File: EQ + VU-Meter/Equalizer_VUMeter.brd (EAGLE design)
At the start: 116 x 38.7 mm, 220 parts, among them IC1 TL074D, IC2 TL074D, IC3 TL074D, IC4 TL074D, T1 BC846A, T10 BC846A, T11 BC846A, T12 BC846A, T13 BC846A, T14 BC846A, T15 BC846A, T16 BC846A, T17 BC846A, T18 BC846A, T19 BC846A, T2 BC846A, T20 BC846A, T21 BC846A, T22 BC846A, T23 BC846A, T24 BC846A, T25 BC846A, T26 BC846A, T27 BC846A, T28 BC846A, T29 BC846A, T3 BC846A, T30 BC846A, T4 BC846A, T5 BC846A, T6 BC846A, T7 BC846A, T8 BC846A, T9 BC846A

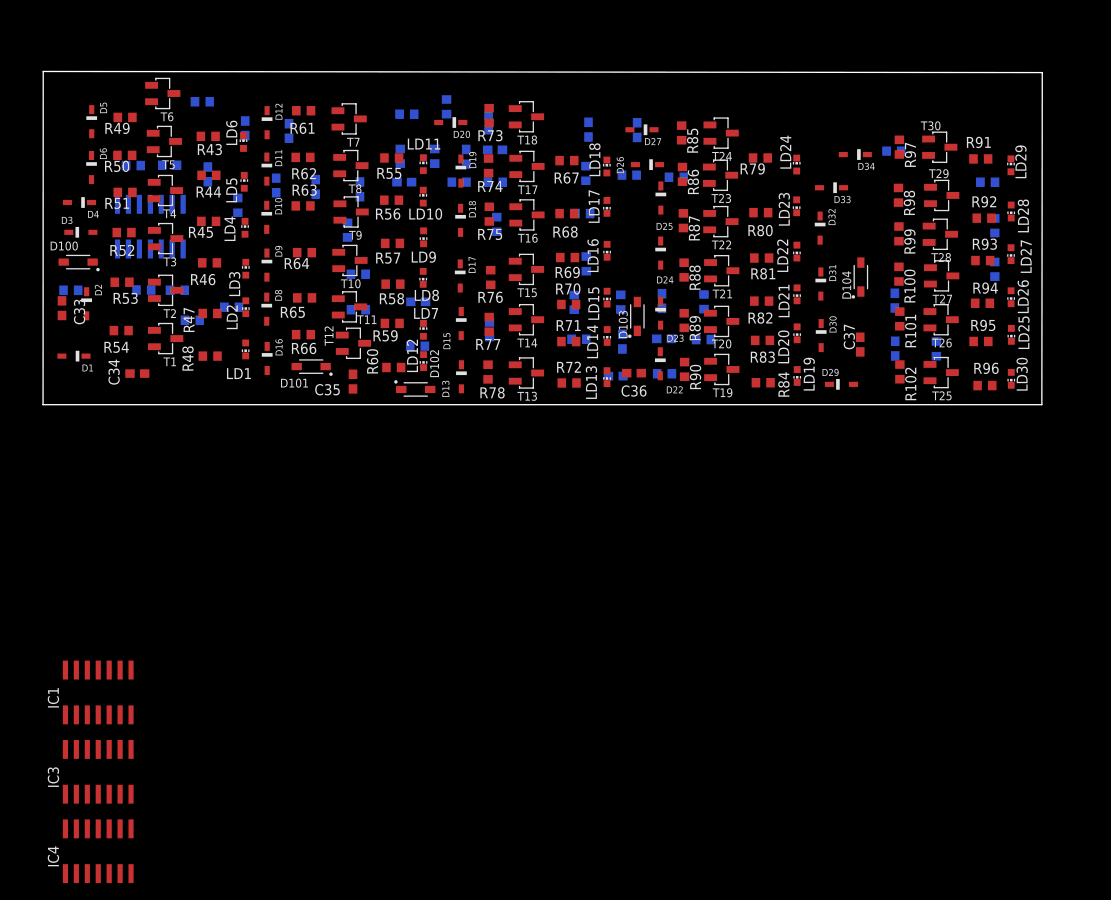
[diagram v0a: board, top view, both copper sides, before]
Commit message: # Mainboard updated
# Keyboard V2:

	# Bug fixed (lowest Pad not GND)
	# 1 more key (upper C)
	# PEACE sign corrected

# General cleanup
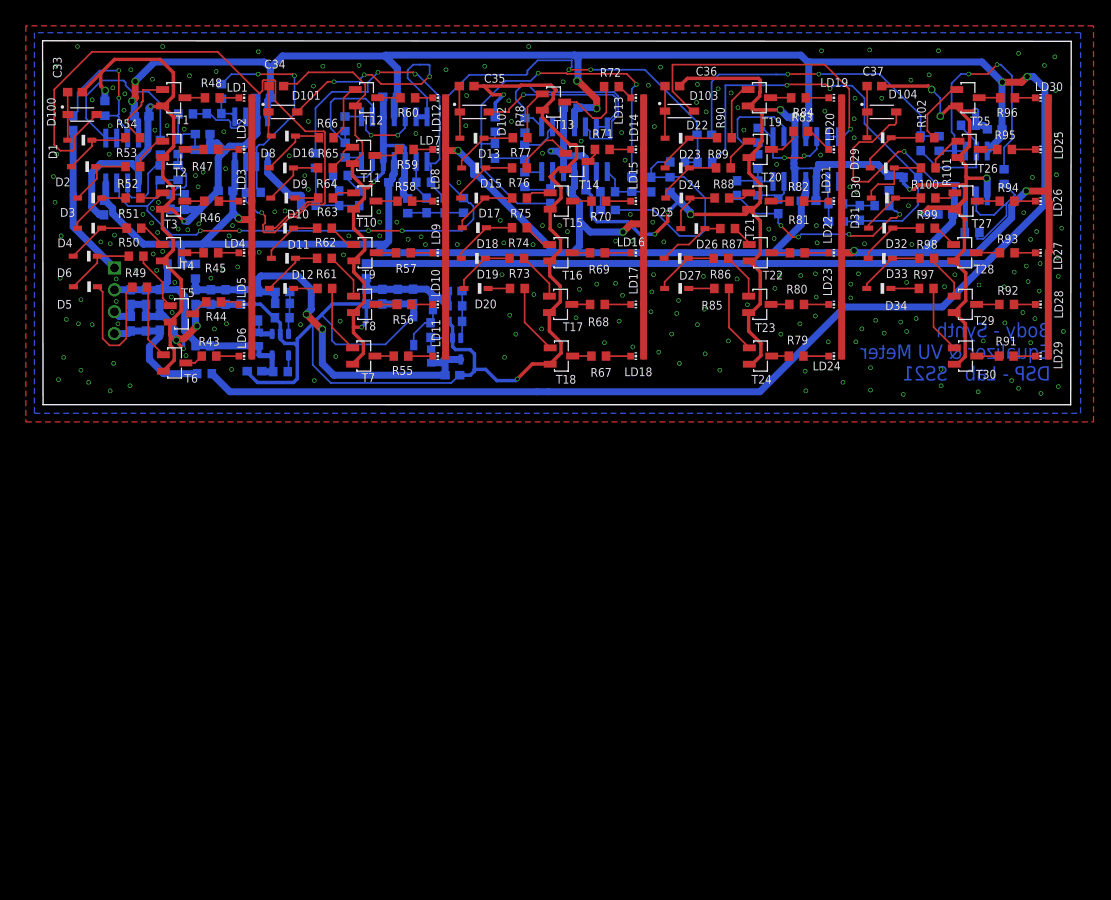
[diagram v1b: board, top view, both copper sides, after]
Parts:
- added C10, C11, C12, C13, C27, C28, C29, C32, C39, C4, C8, C9: 100n, rcl:C0603
- added C14, C40, C41, C42, C43, C44, C45, C46, C47, C48, C49, C50: 10u, rcl:C0603
- added C5: 2.2 uF, rcl:C0603
- added C7: 4.7 uF, rcl:C0603
- added CCUK: 1 uF, rcl:C0603
- added CF: 220 pF, rcl:C0603
- added CFF: 330 pF, rcl:C0603
- added CIN, COUT: 22 uF, rcl:C0603
- added D14, D7: (no value), MMSZ5226B-7-F:SOD3715X135L32X57N
- added IC5, IC7: TL072D, linear:SO08
- added J2: 640455-4, 640455-4:TE_640455-4
- added L1, L2, L3: 10 uH, ASMCI-0603-100M-T:INDC1608X95N
- added R103, R104, R105: 0, rcl:R0603
- added R31: 68 K, rcl:R0603
- added R32: 51K, rcl:R0603
- added R35: 13.3K, rcl:R0603
- added R41: 3.3k, rcl:R0603
- added R42: 35K, rcl:R0603
- added RFB1: 29.4K, rcl:R0603
- added RFB2: 5.76K, rcl:R0603
- added U1: LM2611, LM2611BMFX_NOPB:SOT95P280X145-5N
- added U2: LMR62014, LMR62014XMF_NOPB:SOT95P280X145-5N
- IC1: value TL074D -> TL072D; device linear:SO14 -> linear:SO08
- R26: value 3.3k -> 0
- R27: value 35K -> 0
- moved IC4 115.0 mm to (88.6, 28.5), flipped to the bottom
- moved IC3 91.0 mm to (61.7, 29.7), flipped to the bottom
- moved R27 82.3 mm to (17.7, 15.5), turned to 90 degrees
- moved IC1 66.7 mm to (24.2, 30.8), flipped to the bottom, turned to 180 degrees
- moved R26 45.5 mm to (18.6, 6.85), turned to 180 degrees
- moved R34 41.7 mm to (100.8, 26.4), turned to 180 degrees
- moved C34 37.1 mm to (27.1, 37.0)
- moved C35 36.8 mm to (49.2, 37.0), turned to 0 degrees
- moved R72 34.8 mm to (66.0, 36.9)
- moved R37 34.2 mm to (98.3, 25.7), turned to 270 degrees
- moved C36 33.6 mm to (73.1, 37.0), turned to 0 degrees
- moved R96 33.5 mm to (112.0, 35.6)
- moved R84 33.3 mm to (87.7, 35.6)
- moved D102 32.9 mm to (50.1, 34.0)
- moved LD30 32.8 mm to (116.0, 35.6), turned to 90 degrees
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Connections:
- removed net +8V: IC1.4, IC2.4, IC3.4, IC4.4, LD1.A, LD10.A, LD11.A, LD12.A, LD13.A, LD14.A, LD15.A, LD16.A, LD17.A, LD18.A, LD19.A, LD2.A, LD20.A, LD21.A, LD22.A, LD23.A, LD24.A, LD25.A, LD26.A, LD27.A, LD28.A, LD29.A, LD3.A, LD30.A, LD4.A, LD5.A, LD6.A, LD7.A, LD8.A, LD9.A
- removed net -8V: IC1.11, IC2.11, IC3.11, IC4.11
- removed net 3.3V: C38.2
- removed net N$1: C2.1, C3.1
- removed net N$14: IC3.13, R26.2, R27.1
- removed net N$6: C1.1, C6.1
- removed net TP_OUT1: IC2.8, R6.2
- removed net TP_OUT2: IC3.7, R25.2
- removed net TP_OUT3: IC3.14, R27.2
- new net +7,5V: C45.2, C46.1, C47.1, C7.1, CF.1, CIN.1, D7.1, L2.1, R27.1, R31.2, U1.4, U1.5
- new net -7,5V: C48.2, C49.1, C50.1, CFF.1, COUT.1, L3.2, R105.1, RFB1.1
- new net IN2,1V: C38.2, J2.1
- new net MAIN-5V: C14.2, C43.1, C44.1, J2.4, R103.1
- new net N$100: IC3.12, IC3.8, R25.2
- new net N$115: IC2.12, IC2.8, R6.2
- new net N$126: CCUK.2, D14.2, L3.1
- new net N$141: CCUK.1, L2.2, U1.1
- new net N$152: CFF.2, RFB1.2, RFB2.1, U1.3
- new net N$16: C17.1, R29.2
- new net N$18: C21.1, IC3.7, R18.2, R19.1
- new net N$181: IC2.7, R3.1
- new net N$183: IC4.9, R41.2, R42.1
- new net N$21: R32.1, U2.4
- new net N$22: CF.2, R31.1, R35.1, U2.3
- new net N$25: IC4.12, IC4.8, R42.2
- new net N$48: C25.1, IC4.7, R38.2, R41.1
- new net N$74: D7.2, L1.2, U2.1
- new net PB5V: C40.2, C41.1, C42.1, C5.1, J2.2, L1.1, R104.2, R26.1, R26.2, R32.2, U2.5
- new net V+: C27.1, C28.1, C29.1, C32.1, C39.1, C9.1, IC1.8, IC2.4, IC3.4, IC4.4, IC5.8, IC7.8, LD1.A, LD10.A, LD11.A, LD12.A, LD13.A, LD14.A, LD15.A, LD16.A, LD17.A, LD18.A, LD19.A, LD2.A, LD20.A, LD21.A, LD22.A, LD23.A, LD24.A, LD25.A, LD26.A, LD27.A, LD28.A, LD29.A, LD3.A, LD30.A, LD4.A, LD5.A, LD6.A, LD7.A, LD8.A, LD9.A, R104.1, R27.2
- new net V-: C10.2, C11.2, C12.2, C13.2, C4.2, C8.2, IC1.4, IC2.11, IC3.11, IC4.11, IC5.4, IC7.4, R103.2, R105.2
- net BP1_OUT: now also IC2.13, IC2.14; no longer C17.1, IC2.7, R29.2, R3.1
- net BP2_OUT: now also IC3.13, IC3.14; no longer C21.1, IC3.1, R18.2, R19.1
- net BP3_OUT: now also IC4.13, IC4.14; no longer C25.1, IC4.1, R26.1, R38.2
- net GND: now also C10.1, C11.1, C12.1, C13.1, C14.1, C27.2, C28.2, C29.2, C32.2, C39.2, C4.1, C40.1, C41.2, C42.2, C43.2, C44.2, C45.1, C46.2, C47.2, C48.1, C49.2, C5.2, C50.2, C7.2, C8.1, C9.2, CIN.2, COUT.2, D14.1, IC1.3, IC4.10, IC5.5, IC7.5, J2.3, R35.2, RFB2.2, U1.2, U2.2; no longer IC1.10, IC1.12, IC2.12, IC3.12
- net HP_OUT: now also IC7.7; no longer IC4.7
- net N$10: now also IC1.6; no longer IC1.13
- net N$19: now also IC3.2; no longer IC2.13
- net N$2: now also C1.1, C6.1
- net N$20: now also IC3.1; no longer IC2.14
- net N$24: now also IC3.6; no longer IC3.2
- net N$26: now also IC4.1; no longer IC3.8
- net N$28: now also IC4.2; no longer IC3.9
- net N$29: now also IC5.6; no longer IC1.6
- net N$3: now also IC1.2; no longer IC1.9
- net N$32: now also IC4.6; no longer IC4.2
- net N$34: now also IC7.3; no longer IC4.10
- net N$36: now also IC7.1, IC7.2; no longer IC4.8, IC4.9
- net N$39: now also IC7.6; no longer IC4.6
- net N$4: now also C2.1, C3.1
- net N$42: now also IC5.1, IC5.2; no longer IC1.1, IC1.2
- net N$47: now also IC5.3; no longer IC1.3
- net N$5: now also IC5.7; no longer IC1.7
- net N$8: now also IC1.1; no longer IC1.8
- net N$9: now also IC3.9; no longer IC3.6
- net TP_OUT: now also IC1.7; no longer IC1.14
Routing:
- net GND: track 0.00 -> 577.5 mm, vias 0 -> 21
- net V+: track 0.00 -> 355.1 mm, vias 0 -> 5
- net V-: track 0.00 -> 352.1 mm, vias 0 -> 6
- net N$5: track 0.00 -> 108.3 mm, vias 0 -> 6
- net TP_OUT: track 0.00 -> 80.9 mm, vias 0 -> 1
- net N$27: track 0.00 -> 51.3 mm, vias 0 -> 2
- net N$23: track 0.00 -> 51.1 mm, vias 0 -> 2
- net +7,5V: track 0.00 -> 50.3 mm, vias 0 -> 2
- net N$38: track 0.00 -> 37.4 mm, vias 0 -> 2
- net N$13: track 0.00 -> 37.0 mm, vias 0 -> 2
- net HP_OUT: track 0.00 -> 36.8 mm, vias 0 -> 1
- net BP3_OUT: track 0.00 -> 36.1 mm, vias 0 -> 1
- net PB5V: track 0.00 -> 31.4 mm
- net N$36: track 0.00 -> 30.8 mm, vias 0 -> 2
- net BP1_OUT: track 0.00 -> 29.9 mm, vias 0 -> 3
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- added copper zone on layer 1, net GND
- added copper zone on layer 16, net GND
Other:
- board size 116 x 38.7 mm -> 119.5 x 42.3 mm
- board text added: "Body - Synth Equalizer & VU Meter DSP - Lab SS21"

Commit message: # Mainboard updated V
# Keys finalizing production
# EQ finalizing production
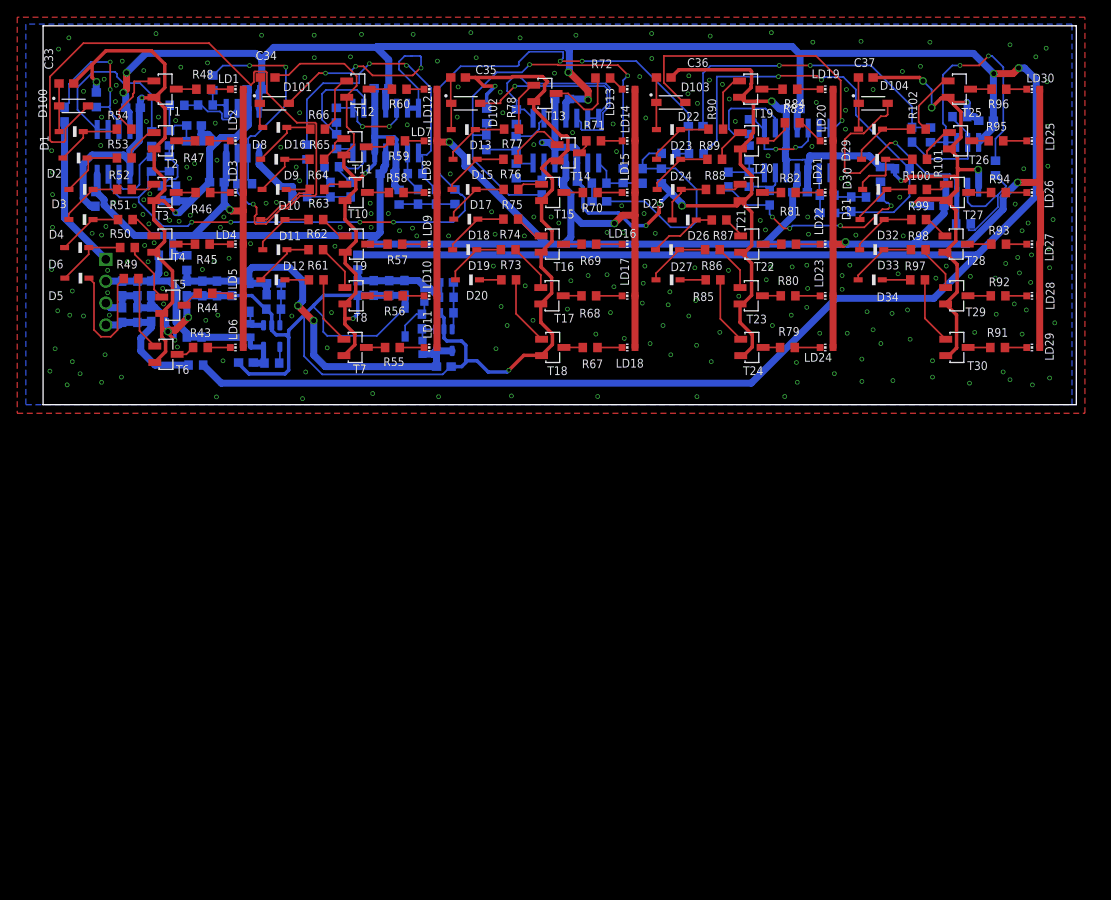
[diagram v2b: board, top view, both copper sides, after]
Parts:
- moved R71 1.41 mm to (63.9, 30.6)
- moved C1 1.41 mm to (17.5, 32.4)
- moved D16 1.41 mm to (26.9, 32.2)
- moved R83 1.41 mm to (87.0, 32.7)
- moved CIN 1.41 mm to (46.5, 4.42)
- moved D1 1.41 mm to (3.27, 31.7)
- moved D2 1.41 mm to (3.71, 28.6)
- moved R32 1.41 mm to (26.6, 4.83)
- moved C10 1.41 mm to (24.6, 36.6)
- moved C11 1.41 mm to (39.3, 36.8)
- moved C12 1.41 mm to (60.3, 35.5)
- moved C13 1.41 mm to (87.1, 34.4)
- moved C14 1.41 mm to (9.18, 10.4)
- moved C15 1.41 mm to (45.6, 24.1)
- moved C16 1.41 mm to (43.5, 24.1)
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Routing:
- net GND: vias 21 -> 22
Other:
- board size 119.5 x 42.3 mm -> 120 x 44 mm
